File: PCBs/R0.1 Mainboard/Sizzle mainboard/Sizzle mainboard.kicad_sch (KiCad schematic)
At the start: 21 parts, among them J1 Spindle relay, J2 Screen, J3 USB_C_Receptacle_USB2.0_16P, J4 Conn_01x06, SW1 SW_Push, U1 STM32F401RCTx, U2 USBLC6-2SC6, Y1 48MHz

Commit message: SilentStepStick
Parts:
- removed J1: Spindle relay, symbol Connector_Generic:Conn_01x02
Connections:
- net SPINDLE_RELAY: no longer names the net of U1.20 (PA4)
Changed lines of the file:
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@@
 		)
 	)
-	(global_label "SPINDLE_RELAY"
+	(global_label "USB_DM"
 		(shape input)
-		(at 264.16 27.94 180)
+		(at 186.69 140.97 0)
 		(fields_autoplaced yes)
 		(effects
@@
 				(size 1.27 1.27)
 			)
-			(justify right)
+			(justify left)
 		)
 		(property "Intersheetrefs" "${INTERSHEET_REFS}"
-			(at 246.721 27.94 0)
-			(effects
-				(font
-					(size 1.27 1.27)
-				)
-				(justify right)
-				(hide yes)
-			)
-		)
-	)
-	(global_label "USB_DM"
+			(at 197.1742 140.97 0)
+			(effects
+				(font
+					(size 1.27 1.27)
+				)
+				(justify left)
+				(hide yes)
+			)
+		)
+	)
+	(global_label "NRST"
 		(shape input)
-		(at 186.69 140.97 0)
+		(at 60.96 60.96 90)
 		(fields_autoplaced yes)
 		(effects
@@
 		)
 		(property "Intersheetrefs" "${INTERSHEET_REFS}"
-			(at 197.1742 140.97 0)
+			(at 60.96 53.1972 90)
 			(effects
 				(font
@@
 		)
 	)
-	(global_label "NRST"
+	(global_label "SWDIO"
 		(shape input)
-		(at 60.96 60.96 90)
+		(at 158.75 100.33 180)
 		(fields_autoplaced yes)
 		(effects
@@
 				(size 1.27 1.27)
 			)
-			(justify left)
+			(justify right)
 		)
 		(property "Intersheetrefs" "${INTERSHEET_REFS}"
-			(at 60.96 53.1972 90)
-			(effects
-				(font
-					(size 1.27 1.27)
-				)
-				(justify left)
-				(hide yes)
-			)
-		)
-	)
-	(global_label "SPINDLE_RELAY"
+			(at 149.8986 100.33 0)
+			(effects
+				(font
+					(size 1.27 1.27)
+				)
+				(justify right)
+				(hide yes)
+			)
+		)
+	)
+	(global_label "SCREEN_TX"
 		(shape output)
-		(at 93.98 78.74 0)
+		(at 93.98 73.66 0)
 		(fields_autoplaced yes)
 		(effects
@@
 		)
 		(property "Intersheetrefs" "${INTERSHEET_REFS}"
-			(at 111.419 78.74 0)
+			(at 107.4879 73.66 0)
 			(effects
 				(font
@@
 		)
 	)
-	(global_label "SWDIO"
+	(global_label "NRST"
 		(shape input)
-		(at 158.75 100.33 180)
+		(at 158.75 92.71 180)
 		(fields_autoplaced yes)
 		(effects
@@
 		)
 		(property "Intersheetrefs" "${INTERSHEET_REFS}"
-			(at 149.8986 100.33 0)
-			(effects
-				(font
-					(size 1.27 1.27)
-				)
-				(justify right)
-				(hide yes)
-			)
-		)
-	)
-	(global_label "SCREEN_TX"
-		(shape output)
-		(at 93.98 73.66 0)
-		(fields_autoplaced yes)
-		(effects
-			(font
-				(size 1.27 1.27)
-			)
-			(justify left)
-		)
-		(property "Intersheetrefs" "${INTERSHEET_REFS}"
-			(at 107.4879 73.66 0)
-			(effects
-				(font
-					(size 1.27 1.27)
-				)
-				(justify left)
-				(hide yes)
-			)
-		)
-	)
-	(global_label "NRST"
-		(shape input)
-		(at 158.75 92.71 180)
-		(fields_autoplaced yes)
-		(effects
-			(font
-				(size 1.27 1.27)
-			)
-			(justify right)
-		)
-		(property "Intersheetrefs" "${INTERSHEET_REFS}"
 			(at 150.9872 92.71 0)
 			(effects
@@
 	)
 	(symbol
-		(lib_id "Connector_Generic:Conn_01x02")
-		(at 269.24 27.94 0)
-		(unit 1)
-		(exclude_from_sim no)
-		(in_bom yes)
-		(on_board yes)
-		(dnp no)
-		(fields_autoplaced yes)
-		(property "Reference" "J1"
-			(at 271.78 27.9399 0)
-			(effects
-				(font
-					(size 1.27 1.27)
-				)
-				(justify left)
-			)
-		)
-		(property "Value" "Spindle relay"
-			(at 271.78 30.4799 0)
-			(effects
-				(font
-					(size 1.27 1.27)
-				)
-				(justify left)
-			)
-		)
-		(property "Footprint" ""
-			(at 269.24 27.94 0)
-			(effects
-				(font
-					(size 1.27 1.27)
-				)
-				(hide yes)
-			)
-		)
-		(property "Datasheet" "~"
-			(at 269.24 27.94 0)
-			(effects
-				(font
-					(size 1.27 1.27)
-				)
-				(hide yes)
-			)
-		)
-		(property "Description" "Generic connector, single row, 01x02, script generated (kicad-library-utils/schlib/autogen/connector/)"
-			(at 269.24 27.94 0)
-			(effects
-				(font
-					(size 1.27 1.27)
-				)
-				(hide yes)
-			)
-		)
-		(pin "2"
-		)
-		(pin "1"
-		)
-		(instances
-			(project ""
-				(path "/ea41cbae-fae8-46a2-97e5-7ea06184cc12"
-					(reference "J1")
-					(unit 1)
-				)
-			)
-		)
-	)
-	(symbol
 		(lib_id "power:GND")
 		(at 77.47 154.94 0)
@@
 					(unit 1)
 				)
-			)
-		)
-	)
-	(symbol
-		(lib_id "power:GND")
-		(at 264.16 30.48 0)
-		(unit 1)
-		(exclude_from_sim no)
-		(in_bom yes)
-		(on_board yes)
-		(dnp no)
-		(fields_autoplaced yes)
-		(property "Reference" "#PWR03"
-			(at 264.16 36.83 0)
-			(effects
-				(font
-					(size 1.27 1.27)
-				)
-				(hide yes)
-			)
-		)
-		(property "Value" "GND"
-			(at 264.16 35.56 0)
-			(effects
-				(font
-					(size 1.27 1.27)
-				)
-				(hide yes)
-			)
-		)
-		(property "Footprint" ""
-			(at 264.16 30.48 0)
-			(effects
-				(font
-					(size 1.27 1.27)
-				)
-				(hide yes)
-			)
-		)
-		(property "Datasheet" ""
-			(at 264.16 30.48 0)
-			(effects
-				(font
-					(size 1.27 1.27)
-				)
-				(hide yes)
-			)
-		)
-		(property "Description" "Power symbol creates a global label with name \"GND\" , ground"
-			(at 264.16 30.48 0)
-			(effects
-				(font
-					(size 1.27 1.27)
-				)
-				(hide yes)
-			)
-		)
-		(pin "1"
-		)
-		(instances
-			(project "Sizzle mainboard"
-				(path "/ea41cbae-fae8-46a2-97e5-7ea06184cc12"
-					(reference "#PWR03")
-					(unit 1)
-				)

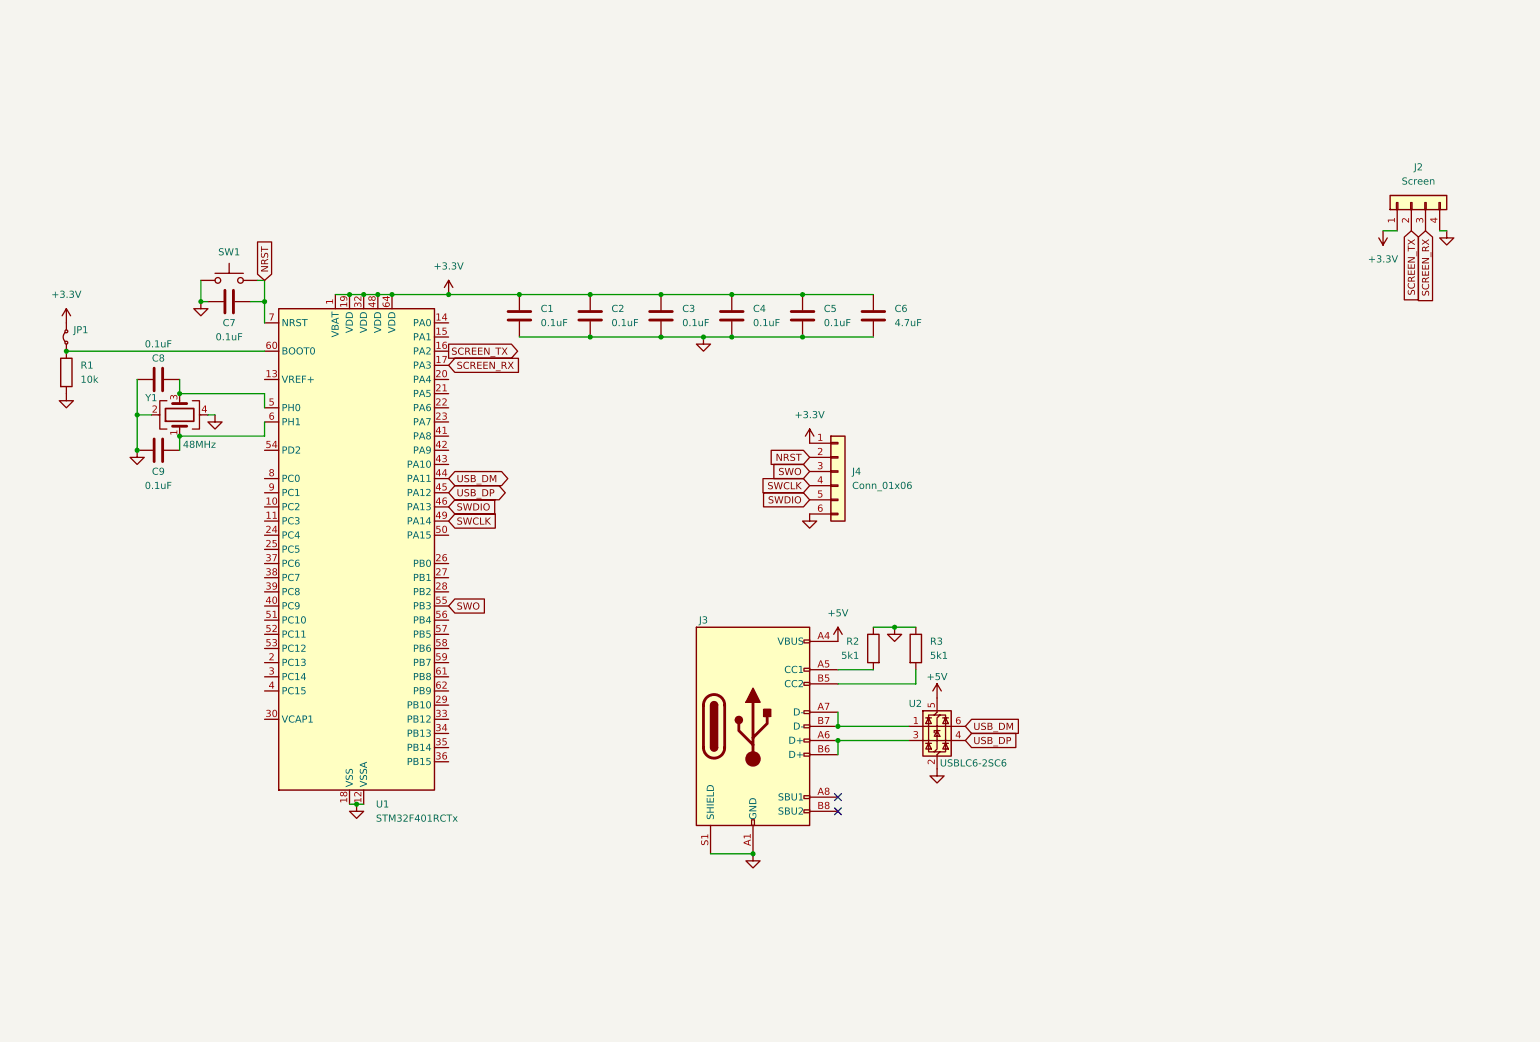
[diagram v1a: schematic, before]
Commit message: cleaned up SilentStepStick and added them to the schematic
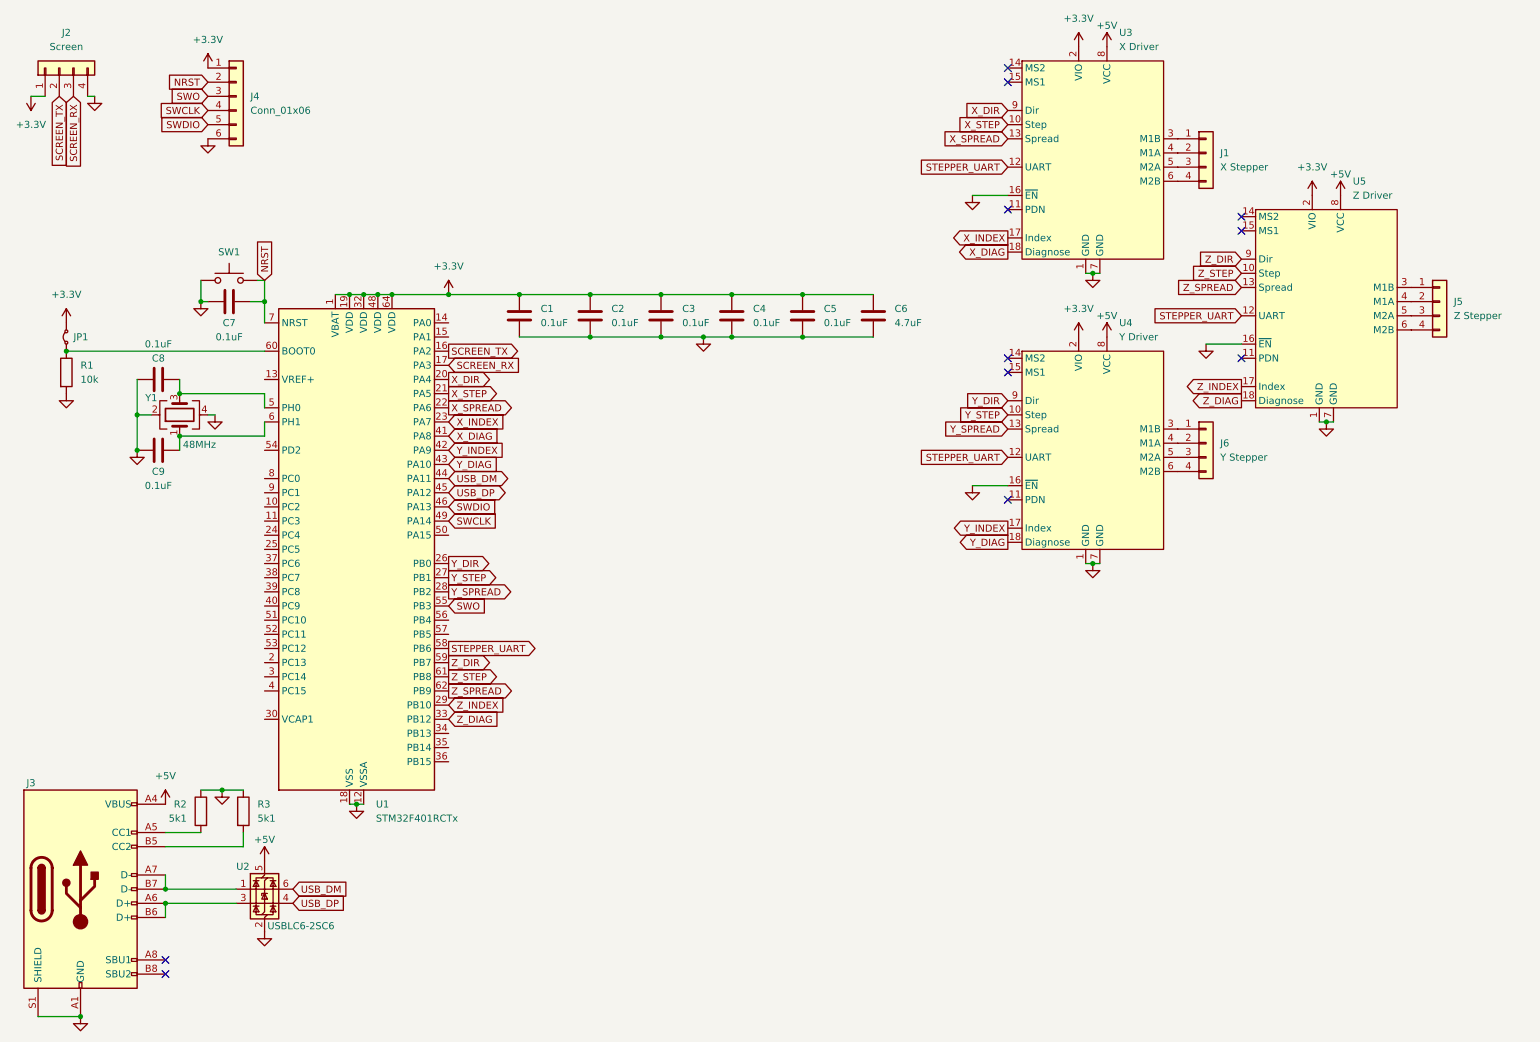
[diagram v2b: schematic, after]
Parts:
- added J1: X Stepper, symbol Connector_Generic:Conn_01x04
- added J5: Z Stepper, symbol Connector_Generic:Conn_01x04
- added J6: Y Stepper, symbol Connector_Generic:Conn_01x04
- added U3: X Driver, symbol Sizzle:TMC2209 SilentStepStick
- added U4: Y Driver, symbol Sizzle:TMC2209 SilentStepStick
- added U5: Z Driver, symbol Sizzle:TMC2209 SilentStepStick
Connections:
- net +3.3V: now also U3.2 (VIO), U4.2 (VIO), U5.2 (VIO)
- net +5V: now also U3.8 (VCC), U4.8 (VCC), U5.8 (VCC)
- net GND: now also U3.1 (GND), U3.16 (~{EN}), U3.7 (GND), U4.1 (GND), U4.16 (~{EN}), U4.7 (GND), U5.1 (GND), U5.16 (~{EN}), U5.7 (GND)
- net X_DIR: now reaches U1.20 (PA4)
- net X_DIR: now also U3.9 (Dir)
- net X_STEP: now reaches U1.21 (PA5)
- net X_STEP: now also U3.10 (Step)
- net X_SPREAD: now reaches U1.22 (PA6)
- net X_SPREAD: now also U3.13 (Spread)
- net X_INDEX: now reaches U1.23 (PA7)
- net X_INDEX: now also U3.17 (Index)
- net Y_DIR: now reaches U1.26 (PB0)
- net Y_DIR: now also U4.9 (Dir)
- net Y_STEP: now reaches U1.27 (PB1)
- net Y_STEP: now also U4.10 (Step)
- net Y_SPREAD: now reaches U1.28 (PB2)
- net Y_SPREAD: now also U4.13 (Spread)
- net Z_INDEX: now reaches U1.29 (PB10)
- net Z_INDEX: now also U5.17 (Index)
- net Z_DIAG: now reaches U1.33 (PB12)
- net Z_DIAG: now also U5.18 (Diagnose)
- net X_DIAG: now reaches U1.41 (PA8)
- net X_DIAG: now also U3.18 (Diagnose)
- net Y_INDEX: now reaches U1.42 (PA9)
- net Y_INDEX: now also U4.17 (Index)
- net Y_DIAG: now reaches U1.43 (PA10)
- net Y_DIAG: now also U4.18 (Diagnose)
- net STEPPER_UART: now reaches U1.58 (PB6)
- net STEPPER_UART: now also U3.12 (UART), U4.12 (UART), U5.12 (UART)
- net Z_DIR: now reaches U1.59 (PB7)
- net Z_DIR: now also U5.9 (Dir)
- net Z_STEP: now reaches U1.61 (PB8)
- net Z_STEP: now also U5.10 (Step)
- net Z_SPREAD: now reaches U1.62 (PB9)
- net Z_SPREAD: now also U5.13 (Spread)
- new net: J5.1 (Pin_1), U5.3 (M1B)
- new net: J5.2 (Pin_2), U5.4 (M1A)
- new net: J5.3 (Pin_3), U5.5 (M2A)
- new net: J5.4 (Pin_4), U5.6 (M2B)
- new net: J1.1 (Pin_1), U3.3 (M1B)
- new net: J1.2 (Pin_2), U3.4 (M1A)
- new net: J1.3 (Pin_3), U3.5 (M2A)
- new net: J1.4 (Pin_4), U3.6 (M2B)
- new net: J6.1 (Pin_1), U4.3 (M1B)
- new net: J6.2 (Pin_2), U4.4 (M1A)
- new net: J6.3 (Pin_3), U4.5 (M2A)
- new net: J6.4 (Pin_4), U4.6 (M2B)
- no-connect marks 2 -> 11
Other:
- moved on the sheet: J2, J3, J4, R2, R3, U2

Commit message: Power
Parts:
- added C10, C11: 1uF, symbol Device:C
- added C12: 0.1uF, symbol Device:C
- added C13: 10uF, symbol Device:C
- added D1: D, symbol Device:D
- added J7: UV light, symbol Connector_Generic:Conn_01x02
- added Q1: Q_NMOS_GSD, symbol Device:Q_NMOS_GSD
- added U6: AP2127R-3.3, Package_TO_SOT_SMD:SOT-89-3, symbol Regulator_Linear:AP2127R-3.3
- added U7: MAX1659ESA, Package_SO:SOIC-8_3.9x4.9mm_P1.27mm, symbol Regulator_Linear:MAX1659ESA
- J4: value Conn_01x06 -> Debug
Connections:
- net +3.3V: now also C11.1, U6.3 (VO); no longer J4.1 (Pin_1)
- net +5V: now also C13.1, D1.1 (K), Q1.2 (S), U7.4 (OUT), U7.5 (OUT); no longer J3.A4 (VBUS), J3.A9 (VBUS), J3.B4 (VBUS), J3.B9 (VBUS), U2.5 (VBUS)
- net GND: now also C10.2, C11.2, C12.2, C13.2, J7.2 (Pin_2), U6.1 (GND), U7.1 (SET), U7.8 (GND)
- net UV_LIGHT: now reaches U1.50 (PA15)
- net UV_LIGHT: now also Q1.1 (G)
- new net: J7.1 (Pin_1), Q1.3 (D)
- new net VBUS: C10.1, D1.2 (A), J3.A4 (VBUS), J3.A9 (VBUS), J3.B4 (VBUS), J3.B9 (VBUS), U2.5 (VBUS), U6.2 (VI)
- new net VDD: C12.1, J4.1 (Pin_1), U7.2 (~{SHTD}), U7.3 (IN), U7.6 (IN), U7.7 (IN)
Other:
- moved on the sheet: C1, C2, C3, C4, C5, C6, C7, C8, C9, JP1, R1, SW1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

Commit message: some power stuff
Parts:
- added D2: D, symbol Device:D
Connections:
- net +3.3V: now also D2.1 (K)
- net VDD: now also D2.2 (A)
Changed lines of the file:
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@@
+	)
+	(symbol
+		(lib_id "Device:D")
+		(at 71.12 26.67 180)
+		(unit 1)
+		(exclude_from_sim no)
+		(in_bom yes)
+		(on_board yes)
+		(dnp no)
+		(fields_autoplaced yes)
+		(property "Reference" "D2"
+			(at 71.12 20.32 0)
+			(effects
+				(font
+					(size 1.27 1.27)
+				)
+			)
+		)
+		(property "Value" "D"
+			(at 71.12 22.86 0)
+			(effects
+				(font
+					(size 1.27 1.27)
+				)
+			)
+		)
+		(property "Footprint" ""
+			(at 71.12 26.67 0)
+			(effects
+				(font
+					(size 1.27 1.27)
+				)
+				(hide yes)
+			)
+		)
+		(property "Datasheet" "~"
+			(at 71.12 26.67 0)
+			(effects
+				(font
+					(size 1.27 1.27)
+				)
+				(hide yes)
+			)
+		)
+		(property "Description" "Diode"
+			(at 71.12 26.67 0)
+			(effects
+				(font
+					(size 1.27 1.27)
+				)
+				(hide yes)
+			)
+		)
+		(property "Sim.Device" "D"
+			(at 71.12 26.67 0)
+			(effects
+				(font
+					(size 1.27 1.27)
+				)
+				(hide yes)
+			)
+		)
+		(property "Sim.Pins" "1=K 2=A"
+			(at 71.12 26.67 0)
+			(effects
+				(font
+					(size 1.27 1.27)
+				)
+				(hide yes)
+			)
+		)
+		(pin "1"
+		)
+		(pin "2"
+		)
+		(instances
+			(project "Sizzle mainboard"
+				(path "/ea41cbae-fae8-46a2-97e5-7ea06184cc12"
+					(reference "D2")
+					(unit 1)
+				)
+			)
+		)
 	)
 	(symbol
@@
 	)
 	(symbol
+		(lib_id "power:+3.3V")
+		(at 74.93 26.67 0)
+		(unit 1)
+		(exclude_from_sim no)
+		(in_bom yes)
+		(on_board yes)
+		(dnp no)
+		(fields_autoplaced yes)
+		(property "Reference" "#PWR041"
+			(at 74.93 30.48 0)
+			(effects
+				(font
+					(size 1.27 1.27)
+				)
+				(hide yes)
+			)
+		)
+		(property "Value" "+3.3V"
+			(at 74.93 21.59 0)
+			(effects
+				(font
+					(size 1.27 1.27)
+				)
+			)
+		)
+		(property "Footprint" ""
+			(at 74.93 26.67 0)
+			(effects
+				(font
+					(size 1.27 1.27)
+				)
+				(hide yes)
+			)
+		)
+		(property "Datasheet" ""
+			(at 74.93 26.67 0)
+			(effects
+				(font
+					(size 1.27 1.27)
+				)
+				(hide yes)
+			)
+		)
+		(property "Description" "Power symbol creates a global label with name \"+3.3V\""
+			(at 74.93 26.67 0)
+			(effects
+				(font
+					(size 1.27 1.27)
+				)
+				(hide yes)
+			)
+		)
+		(pin "1"
+		)
+		(instances
+			(project "Sizzle mainboard"
+				(path "/ea41cbae-fae8-46a2-97e5-7ea06184cc12"
+					(reference "#PWR041")
+					(unit 1)
+				)
+			)
+		)
+	)
+	(symbol
 		(lib_id "power:VBUS")
 		(at 43.18 154.94 0)
@@
 					(unit 1)
 				)
+			)
+		)
+	)
+	(symbol
+		(lib_id "power:VDD")
+		(at 67.31 26.67 0)
+		(unit 1)
+		(exclude_from_sim no)
+		(in_bom yes)
+		(on_board yes)
+		(dnp no)
+		(fields_autoplaced yes)
+		(property "Reference" "#PWR040"
+			(at 67.31 30.48 0)
+			(effects
+				(font
+					(size 1.27 1.27)
+				)
+				(hide yes)
+			)
+		)
+		(property "Value" "VDD"
+			(at 67.31 21.59 0)
+			(effects
+				(font
+					(size 1.27 1.27)
+				)
+			)
+		)
+		(property "Footprint" ""
+			(at 67.31 26.67 0)
+			(effects
+				(font
+					(size 1.27 1.27)
+				)
+				(hide yes)
+			)
+		)
+		(property "Datasheet" ""
+			(at 67.31 26.67 0)
+			(effects
+				(font
+					(size 1.27 1.27)
+				)
+				(hide yes)
+			)
+		)
+		(property "Description" "Power symbol creates a global label with name \"VDD\""
+			(at 67.31 26.67 0)
+			(effects
+				(font
+					(size 1.27 1.27)
+				)
+				(hide yes)
+			)
+		)
+		(pin "1"
+		)
+		(instances
+			(project "Sizzle mainboard"
+				(path "/ea41cbae-fae8-46a2-97e5-7ea06184cc12"
+					(reference "#PWR040")
+					(unit 1)
+				)
